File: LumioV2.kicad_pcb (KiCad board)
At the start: 2 copper layers, 83 parts, among them J1 I2C POINT 1 - QWIIC, J10 MOTOR B, J11 Analog Input, J12 Analog Input, J13 Analog Input, J14 Analog Input, J15 Analog Input, J16 Analog Input, J17 Analog Input, J18 Analog Input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

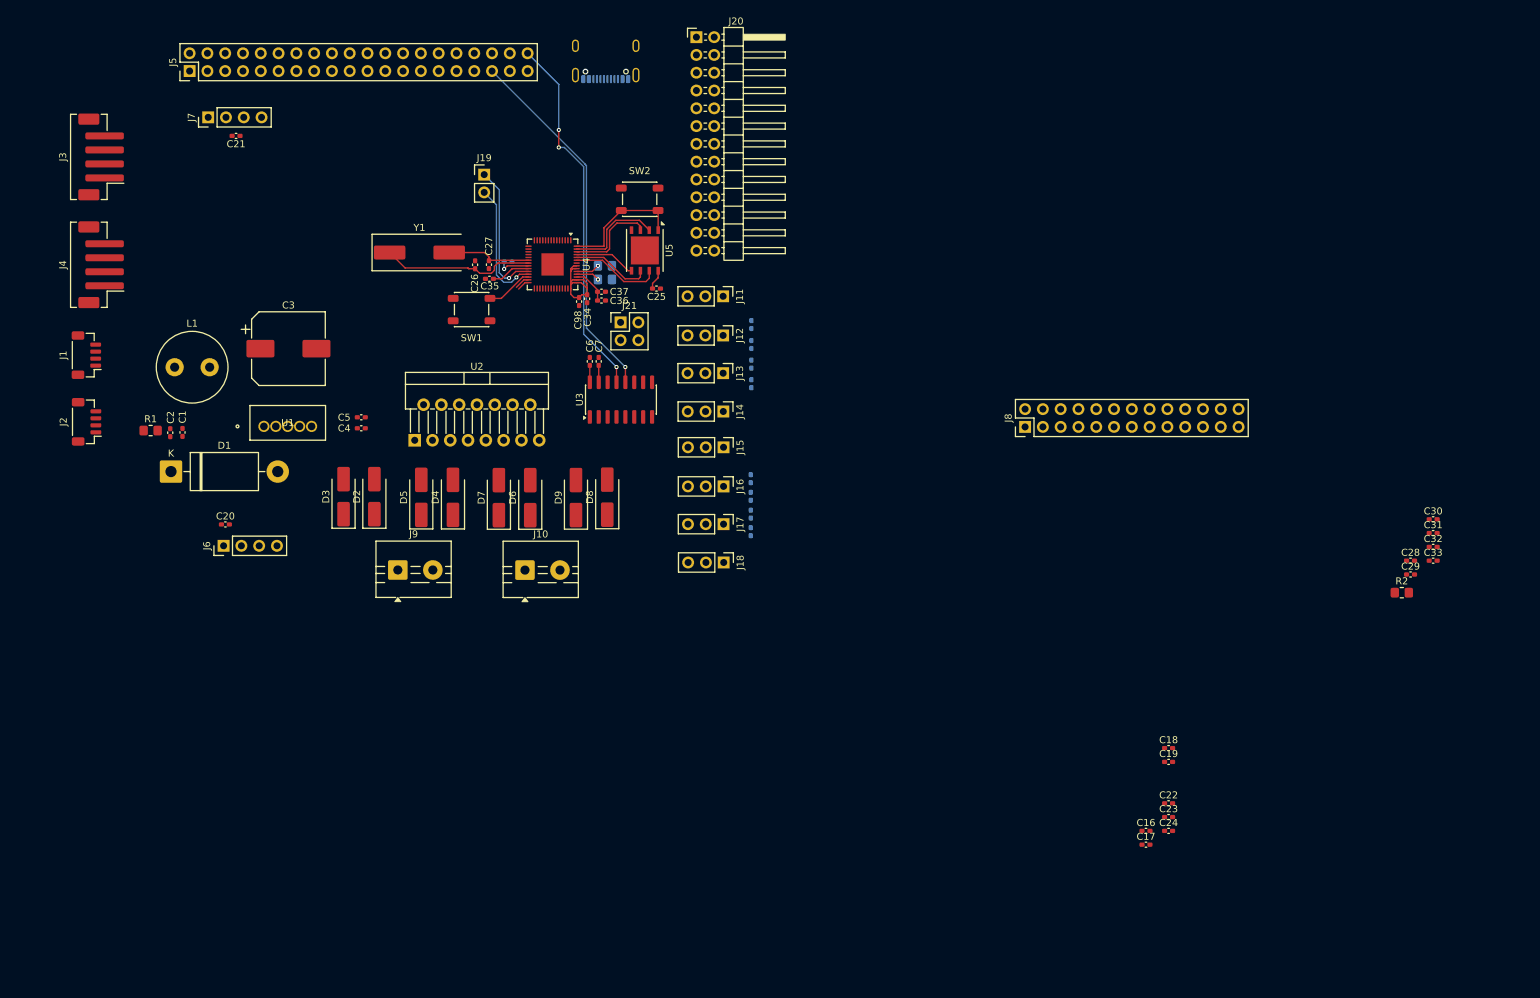
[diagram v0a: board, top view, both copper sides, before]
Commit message: re-started routing, for clearer routes. also moved to dsi conenctor for display
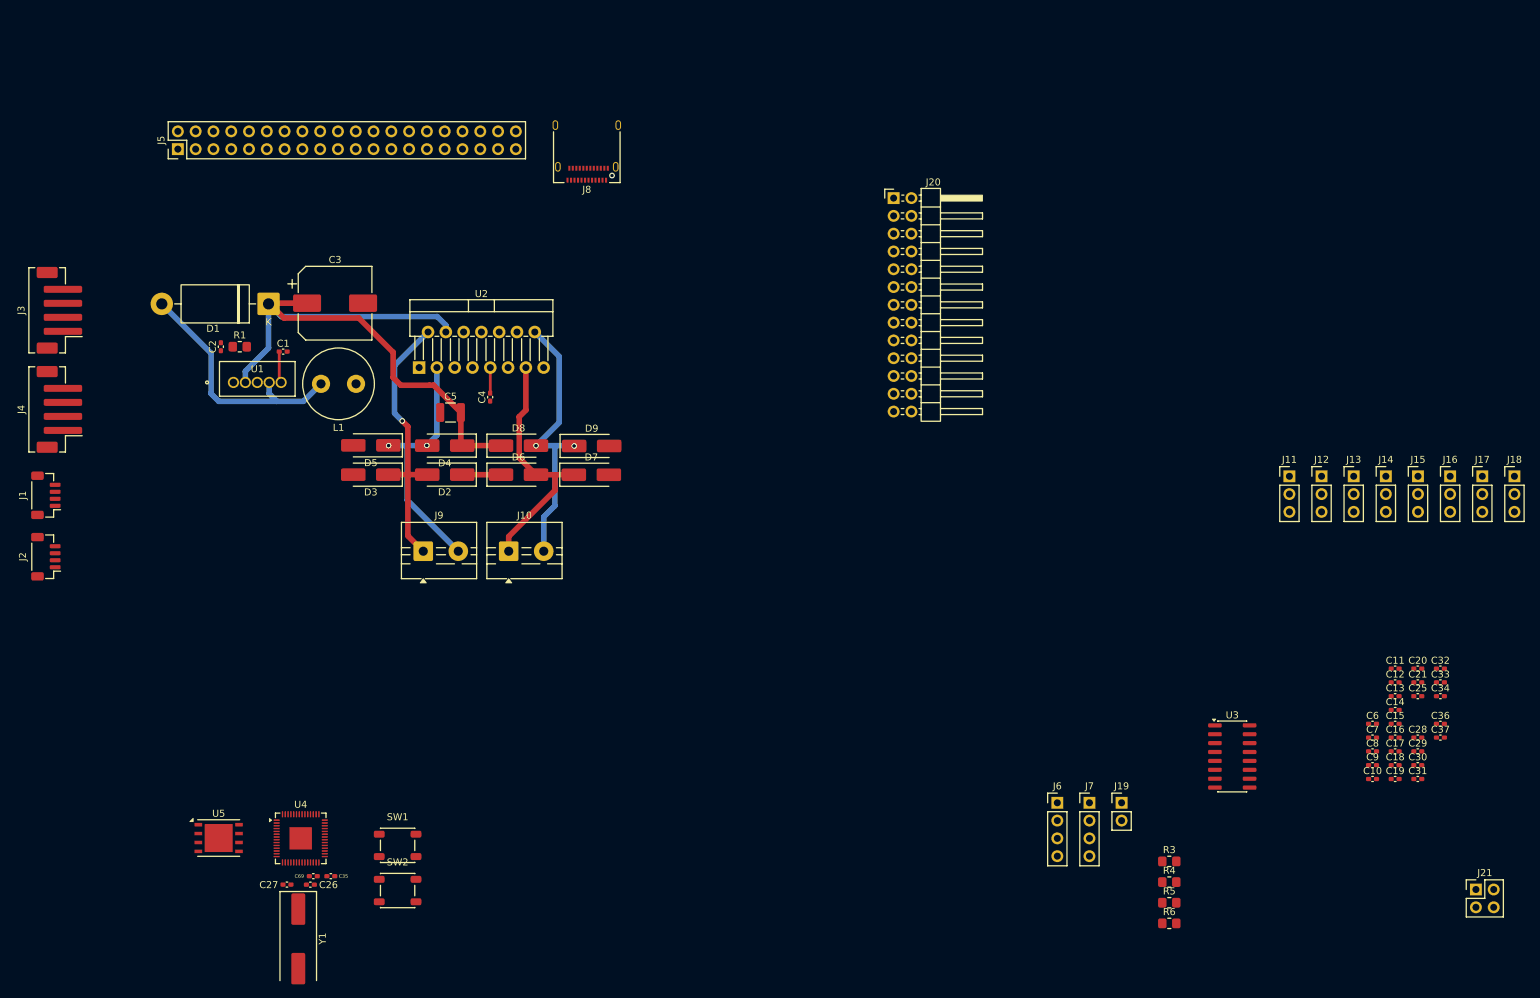
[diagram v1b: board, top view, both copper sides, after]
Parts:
- removed C22, C23, C24: 100nF, Capacitor_SMD:C_0402_1005Metric_Pad0.74x0.62mm_HandSolder
- removed C98, C99: 1uF, Capacitor_SMD:C_0402_1005Metric_Pad0.74x0.62mm_HandSolder
- removed P1: USB_C_Plug_USB2.0, Connector_USB:USB_C_Receptacle_GCT_USB4105-xx-A_16P_TopMnt_Horizontal
- removed R2: 5.1K, Resistor_SMD:R_0805_2012Metric_Pad1.20x1.40mm_HandSolder
- added C69: 1uF, Capacitor_SMD:C_0402_1005Metric_Pad0.74x0.62mm_HandSolder, F.Cu at (99.3, 148.4)
- added R5: 5.1K, Resistor_SMD:R_0805_2012Metric_Pad1.20x1.40mm_HandSolder, F.Cu at (221.5, 152.2)
- added R6: 5.1K, Resistor_SMD:R_0805_2012Metric_Pad1.20x1.40mm_HandSolder, F.Cu at (221.5, 155.1)
- C10, C11, C12, C13, C14, C15, C8, C9, R3, R4: moved to F.Cu
- C5: footprint Capacitor_SMD:C_0402_1005Metric_Pad0.74x0.62mm_HandSolder -> Capacitor_SMD:C_1210_3225Metric
- J8: value Display Connector -> USB_C_Receptacle_USB2.0_14P; footprint Connector_PinHeader_2.54mm:PinHeader_2x13_P2.54mm_Vertical -> Connector_USB:USB_C_Receptacle_Amphenol_12401610E4-2A
- moved C21 185.9 mm to (257.0, 120.7), turned to 0 degrees
- moved C20 171.5 mm to (257.0, 118.8), turned to 0 degrees
- moved J7 159.4 mm to (210.1, 137.9), turned to 0 degrees
- moved J21 146.5 mm to (265.3, 150.3)
- moved C37 135.6 mm to (260.2, 128.6), turned to 0 degrees
- moved C34 134.4 mm to (260.2, 122.7), turned to 0 degrees
- moved C36 134.2 mm to (260.2, 126.6), turned to 0 degrees
- moved J19 127.8 mm to (214.7, 137.9)
- moved J6 124.6 mm to (205.5, 137.9), turned to 0 degrees
- moved C25 123.3 mm to (257.0, 122.7), turned to 0 degrees
- moved C6 123.2 mm to (250.5, 126.6), turned to 0 degrees
- moved C7 122.9 mm to (250.5, 128.6), turned to 0 degrees
- moved R4 119.3 mm to (221.5, 149.2)
- moved R3 115.7 mm to (221.5, 146.3), turned to 0 degrees
- moved J18 113.6 mm to (270.8, 91.3), turned to 0 degrees
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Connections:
- J5 pad 10: unconnected-(J5-Pin_10-Pad10) -> Net-(J20-Pin_1)
- J5 pad 18: Net-(J5-Pin_18) -> unconnected-(J5-Pin_18-Pad18)
- J5 pad 19: Net-(J5-Pin_19) -> unconnected-(J5-Pin_19-Pad19)
- J5 pad 21: Net-(J5-Pin_21) -> unconnected-(J5-Pin_21-Pad21)
- J5 pad 22: Net-(J5-Pin_22) -> unconnected-(J5-Pin_22-Pad22)
- J5 pad 23: Net-(J5-Pin_23) -> unconnected-(J5-Pin_23-Pad23)
- J5 pad 24: Net-(J5-Pin_24) -> unconnected-(J5-Pin_24-Pad24)
- J5 pad 26: Net-(J5-Pin_26) -> unconnected-(J5-Pin_26-Pad26)
- J5 pad 8: unconnected-(J5-Pin_8-Pad8) -> Net-(J20-Pin_2)
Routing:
- net Net-(D1-K): track 0.00 -> 97.6 mm
- net Net-(J5-Pin_40): track 52.8 -> 0.00 mm, vias 3 -> 0
- net Net-(J5-Pin_35): track 52.3 -> 0.00 mm, vias 1 -> 0
- net Net-(D2-A): track 0.00 -> 40.5 mm, vias 0 -> 1
- net Net-(D8-A): track 0.00 -> 40.3 mm, vias 0 -> 2
- net Net-(D1-A): track 0.00 -> 36.1 mm
- net Net-(D6-A): track 0.00 -> 35.7 mm
- net Net-(D4-A): track 0.00 -> 35.3 mm, vias 0 -> 2
- net +3V3: track 25.1 -> 0.00 mm, vias 1 -> 0
- net Net-(U4-XOUT): track 22.1 -> 0.00 mm
- net Net-(J19-Pin_1): track 19.8 -> 0.00 mm, vias 1 -> 0
- net Net-(U4-~{QSPI_SS}): track 18.1 -> 0.00 mm
- net Net-(J19-Pin_2): track 18.0 -> 0.00 mm, vias 1 -> 0
- net Net-(U4-QSPI_SD1): track 14.2 -> 0.00 mm
- net Net-(U4-QSPI_SD2): track 13.1 -> 0.00 mm
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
